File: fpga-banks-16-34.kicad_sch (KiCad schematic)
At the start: 40 parts, among them J8 PinHeader_2x4_P2.54mm_Drill1mm, U13 Oscillator_SMD_100MHz_ASFLMB, U14 TCA39306_VSSOP, U8 XC7K160T-FFG676

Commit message: [#80386] Update Manufacturer of FPGA chip
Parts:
- U8: Manufacturer Xilinx -> AMD-Xilinx
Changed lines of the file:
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@@
 			)
 		)
-		(property "Description" ""
+		(property "Description" "FPGA Kintex-7 Family 162240 Cells 28nm Technology"
 			(at 45.72 71.12 0)
 			(effects
@@
 			)
 		)
-		(property "Manufacturer" "Xilinx"
+		(property "Manufacturer" "AMD-Xilinx"
 			(at 45.72 71.12 0)
 			(effects
@@
 			)
 		)
-		(property "Description" ""
+		(property "Description" "FPGA Kintex-7 Family 162240 Cells 28nm Technology"
 			(at 243.205 71.755 0)
 			(effects
@@
 			)
 		)
-		(property "Manufacturer" "Xilinx"
+		(property "Manufacturer" "AMD-Xilinx"
 			(at 243.205 71.755 0)
 			(effects
@@
 			)
 		)
-		(property "Description" ""
+		(property "Description" "FPGA Kintex-7 Family 162240 Cells 28nm Technology"
 			(at 124.46 69.85 0)
 			(effects
@@
 			)
 		)
-		(property "Manufacturer" "Xilinx"
+		(property "Manufacturer" "AMD-Xilinx"
 			(at 124.46 69.85 0)
 			(effects
@@
 			)
 		)
-		(property "Description" ""
+		(property "Description" "FPGA Kintex-7 Family 162240 Cells 28nm Technology"
 			(at 325.755 71.755 0)
 			(effects
@@
 			)
 		)
-		(property "Manufacturer" "Xilinx"
+		(property "Manufacturer" "AMD-Xilinx"
 			(at 325.755 71.755 0)
 			(effects

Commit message: [#80386] Add company name in board settings
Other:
- company: Antmicro Ltd. -> Antmicro
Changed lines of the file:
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@@
 		(date "2023-07-27")
 		(rev "1.0.1")
-		(company "Antmicro Ltd.")
+		(company "Antmicro")
 		(comment 1 "www.antmicro.com")
-		(comment 2 "Antmicro Ltd")
 	)
 	(text "Clock source"

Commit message: [#87036] Update components, clear DRC and ERC
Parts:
- C168, C169, C170, C171, C172, C173, C174, C175, C176: footprint data-center-rdimm-ddr5-tester-footprints:C_0402_1005Metric -> antmicro-footprints:C_0402_1005Metric; symbol data-center-rdimm-ddr5-tester:C_100n_6V3_0402 -> antmicroCapacitorsmisc:C_100n_6V3_0402; Public (none) -> False
- FB10, FB11, FB9: footprint data-center-rdimm-ddr5-tester-footprints:FB_0402_1005Metric -> antmicro-footprints:FB_0402_1005Metric; symbol data-center-rdimm-ddr5-tester:FB_600Z_0.3A_0402 -> antmicroFerriteBeadsandChips:FB_600Z_0.3A_Murata-BLM15AG_0402; Val (none) -> 600Z/0.3A
- J8: DNP DNP -> (none); now not fitted; now left out of the parts list
- R124, R125, R128, R129, R159, R160: footprint data-center-rdimm-ddr5-tester-footprints:R_0603_1608Metric -> antmicro-footprints:R_0603_1608Metric; symbol data-center-rdimm-ddr5-tester:R_1k_0603 -> antmicroResistors0603:R_1k_0603
- R126, R127, R130, R131, R161, R162: footprint data-center-rdimm-ddr5-tester-footprints:R_0603_1608Metric -> antmicro-footprints:R_0603_1608Metric; symbol data-center-rdimm-ddr5-tester:R_120R_0603 -> antmicroResistors0603:R_120R_0603
- R132: footprint data-center-rdimm-ddr5-tester-footprints:R_0402_1005Metric -> antmicro-footprints:R_0402_1005Metric; symbol data-center-rdimm-ddr5-tester:R_200k_0402 -> antmicroResistors0402:R_200k_0402
- R133, R135, R136, R137, R138, R139, R140: footprint data-center-rdimm-ddr5-tester-footprints:R_0402_1005Metric -> antmicro-footprints:R_0402_1005Metric; symbol data-center-rdimm-ddr5-tester:R_0R_0402 -> antmicroResistors0402:R_0R_0402
- R171, R172, R173, R174: footprint data-center-rdimm-ddr5-tester-footprints:R_0402_1005Metric -> antmicro-footprints:R_0402_1005Metric; symbol data-center-rdimm-ddr5-tester:R_4k7_0402 -> antmicroResistors0402:R_4k7_0402
- U13: footprint data-center-rdimm-ddr5-tester-footprints:Oscillator_SMD_Abracon_ASFLMB_5x3.2x0.85mm -> antmicro-footprints:Oscillator_SMD_Abracon_ASFLMB_5x3.2x0.85mm; symbol data-center-rdimm-ddr5-tester:Oscillator_SMD_100MHz_ASFLMB -> antmicroOscillators:Oscillator_100MHz_ASFLMB; Val (none) -> 100 MHz
- U14: footprint data-center-rdimm-ddr5-tester-footprints:VSSOP-8_2.3x2mm_P0.5mm -> antmicro-footprints:VSSOP-8_2.3x2mm_P0.5mm; symbol data-center-rdimm-ddr5-tester:TCA39306_VSSOP -> antmicroLogicTranslatorsLevelShifters:TCA39306_VSSOP
- U8: footprint data-center-rdimm-ddr5-tester-footprints:BGA-676_27x27mm_Layout26x26_P1X1mm -> antmicro-footprints:BGA-676_27x27mm_Layout26x26_P1x1mm_FFG676; symbol data-center-rdimm-ddr5-tester:XC7K160T-FFG676 -> antmicroFPGAChips:XC7K160T-FFG676
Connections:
- net 1V0_SYS renamed +1V0
- net 1V1_SYS renamed +1V1
- net 3V3_SYS renamed +3V3
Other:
- moved on the sheet: C168, C171, C172, R124, R125, R126, R127, R130, R131, R132, R133, R135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

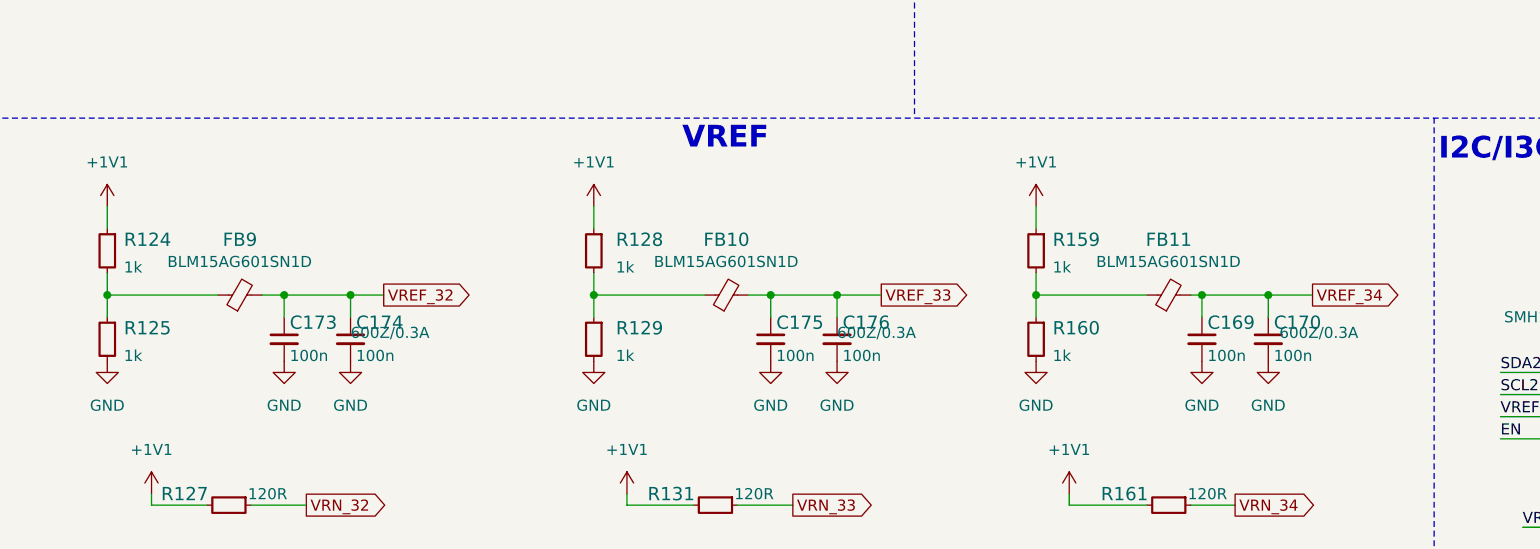
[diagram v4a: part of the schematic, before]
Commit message: [#87036] Add ICT testpoints
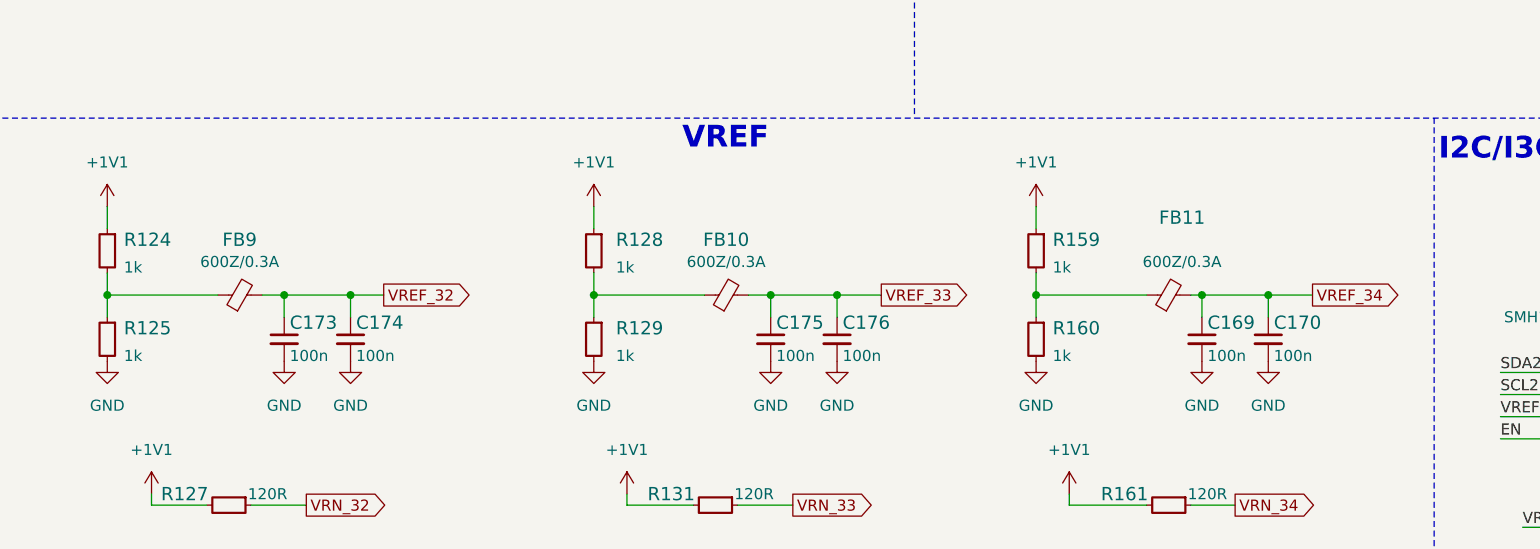
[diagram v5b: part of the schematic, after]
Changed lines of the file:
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@@
 		(on_board yes)
 		(dnp no)
+		(fields_autoplaced yes)
 		(property "Reference" "FB9"
-			(at 119.38 236.22 0)
+			(at 119.3419 236.22 0)
 			(effects
 				(font
@@
 		)
 		(property "MPN" "BLM15AG601SN1D"
-			(at 119.3419 238.76 0)
-			(effects
-				(font
-					(size 1.27 1.27)
-					(thickness 0.15)
-				)
+			(at 119.3419 236.22 0)
+			(effects
+				(font
+					(size 1.27 1.27)
+					(thickness 0.15)
+				)
+				(hide yes)
 			)
 		)
@@
 		)
 		(property "Val" "600Z/0.3A"
-			(at 132.08 247.65 0)
-			(effects
-				(font
-					(size 1.27 1.27)
-				)
-				(justify left bottom)
+			(at 119.3419 238.76 0)
+			(effects
+				(font
+					(size 1.27 1.27)
+				)
 			)
 		)
@@
 		(on_board yes)
 		(dnp no)
+		(fields_autoplaced yes)
 		(property "Reference" "FB10"
-			(at 175.26 236.22 0)
+			(at 175.2219 236.22 0)
 			(effects
 				(font
@@
 		)
 		(property "MPN" "BLM15AG601SN1D"
-			(at 175.2219 238.76 0)
-			(effects
-				(font
-					(size 1.27 1.27)
-					(thickness 0.15)
-				)
+			(at 175.2219 236.22 0)
+			(effects
+				(font
+					(size 1.27 1.27)
+					(thickness 0.15)
+				)
+				(hide yes)
 			)
 		)
@@
 		)
 		(property "Val" "600Z/0.3A"
-			(at 187.96 247.65 0)
-			(effects
-				(font
-					(size 1.27 1.27)
-				)
-				(justify left bottom)
+			(at 175.2219 238.76 0)
+			(effects
+				(font
+					(size 1.27 1.27)
+				)
 			)
 		)
@@
 		(dnp no)
 		(property "Reference" "FB11"
-			(at 226.06 236.22 0)
+			(at 227.584 233.68 0)
 			(effects
 				(font
@@
 		)
 		(property "MPN" "BLM15AG601SN1D"
-			(at 226.0219 238.76 0)
-			(effects
-				(font
-					(size 1.27 1.27)
-					(thickness 0.15)
-				)
+			(at 227.584 236.22 0)
+			(effects
+				(font
+					(size 1.27 1.27)
+					(thickness 0.15)
+				)
+				(hide yes)
 			)
 		)
@@
 		)
 		(property "Val" "600Z/0.3A"
-			(at 238.76 247.65 0)
-			(effects
-				(font
-					(size 1.27 1.27)
-				)
-				(justify left bottom)
-			)
-		)
+			(at 227.584 238.76 0)
+			(effects
+				(font
+					(size 1.27 1.27)
+				)
+			)
+		)
